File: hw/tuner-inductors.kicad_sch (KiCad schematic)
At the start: 19 parts, among them K1701 G2RL-2, K1702 G2RL-2, K1703 G2RL-2, K1704 G2RL-2, K1705 G2RL-2, K1706 G2RL-2, K1707 G2RL-2, U1701 TPIC6C595PWR

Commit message: I think I have finished the relay conversion and 5V SPI I/O expander crap
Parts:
- removed C1701, C1702, C1703: 10uF, Capacitor_SMD:C_0805_2012Metric, symbol Device:C
- removed K1701, K1702, K1703, K1704, K1705, K1706, K1707: G2RL-2, Library:Relay_DPDT_Omron_G2RL-2, symbol Library:G2RL-2-functional
- removed L1706: 1uH, Library:Coilcraft-uni10, symbol Device:L_Small
- added D7707, D7708, D7709, D7710, D7711, D7712, D7713: 1N4148W, Diode_SMD:D_SOD-123, symbol Diode:1N4148W
- added K7718, K7719, K7720, K7721, K7722, K7723, K7724: G5Q-14-05, Relay_THT:Relay_SPDT_Omron-G5Q-1, symbol Relay:G5Q-1
- added L7730: 1uH, Library:Coilcraft-uni10, symbol Device:L_Small
- renumbered C7720 to C7890, L1701 to L7725, L1702 to L7726, L1703 to L7727, L1704 to L7728, L1705 to L7729, L1707 to L7731, U1701 to U7741
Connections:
- net +5V: now also D7707.1 (K), D7708.1 (K), D7709.1 (K), D7710.1 (K), D7711.1 (K), D7712.1 (K), D7713.1 (K), K7718.5, K7719.5, K7720.5, K7721.5, K7722.5, K7723.5, K7724.5
- net Lcold: now also K7724.4
- net Lhot: now also K7718.2
- net L4: now reaches U7741.11 (DRAIN4)
- net L4: now also D7709.2 (A), K7720.1
- net at L7725.2, L7726.1: now also K7718.4, K7719.2
- net at L7726.2, L7727.1: now also K7719.4, K7720.2
- net at L7728.2, L7729.1: now also K7721.4, K7722.2
- net at L7729.2: now also K7722.4, K7723.2, L7730.1
- net L6: now reaches U7741.13 (DRAIN6)
- net at L7731.1: now also K7723.4, K7724.2, L7730.2
- net at L7727.2, L7728.1: now also K7720.4, K7721.2
- net L5: now reaches U7741.12 (DRAIN5)
- net L5: now also D7708.2 (A), K7719.1
- net L0: now reaches U7741.3 (DRAIN0)
- net L0: now also D7713.2 (A), K7724.1
- net L1: now reaches U7741.4 (DRAIN1)
- net L1: now also D7712.2 (A), K7723.1
- net L2: now reaches U7741.5 (DRAIN2)
- net L2: now also D7711.2 (A), K7722.1
- net L3: now reaches U7741.6 (DRAIN3)
- net L3: now also D7710.2 (A), K7721.1
- new net: D7707.2 (A), K7718.1
- no-connect marks 29 -> 8
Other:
- note removed: "L0"
- note removed: "L1"
- note removed: "L2"
- note removed: "L3"
- note removed: "L4"
- note removed: "L5"
- note removed: "L6"
- moved on the sheet: C7890, L7725, L7726, L7727, L7728, L7729, L7731, U7741

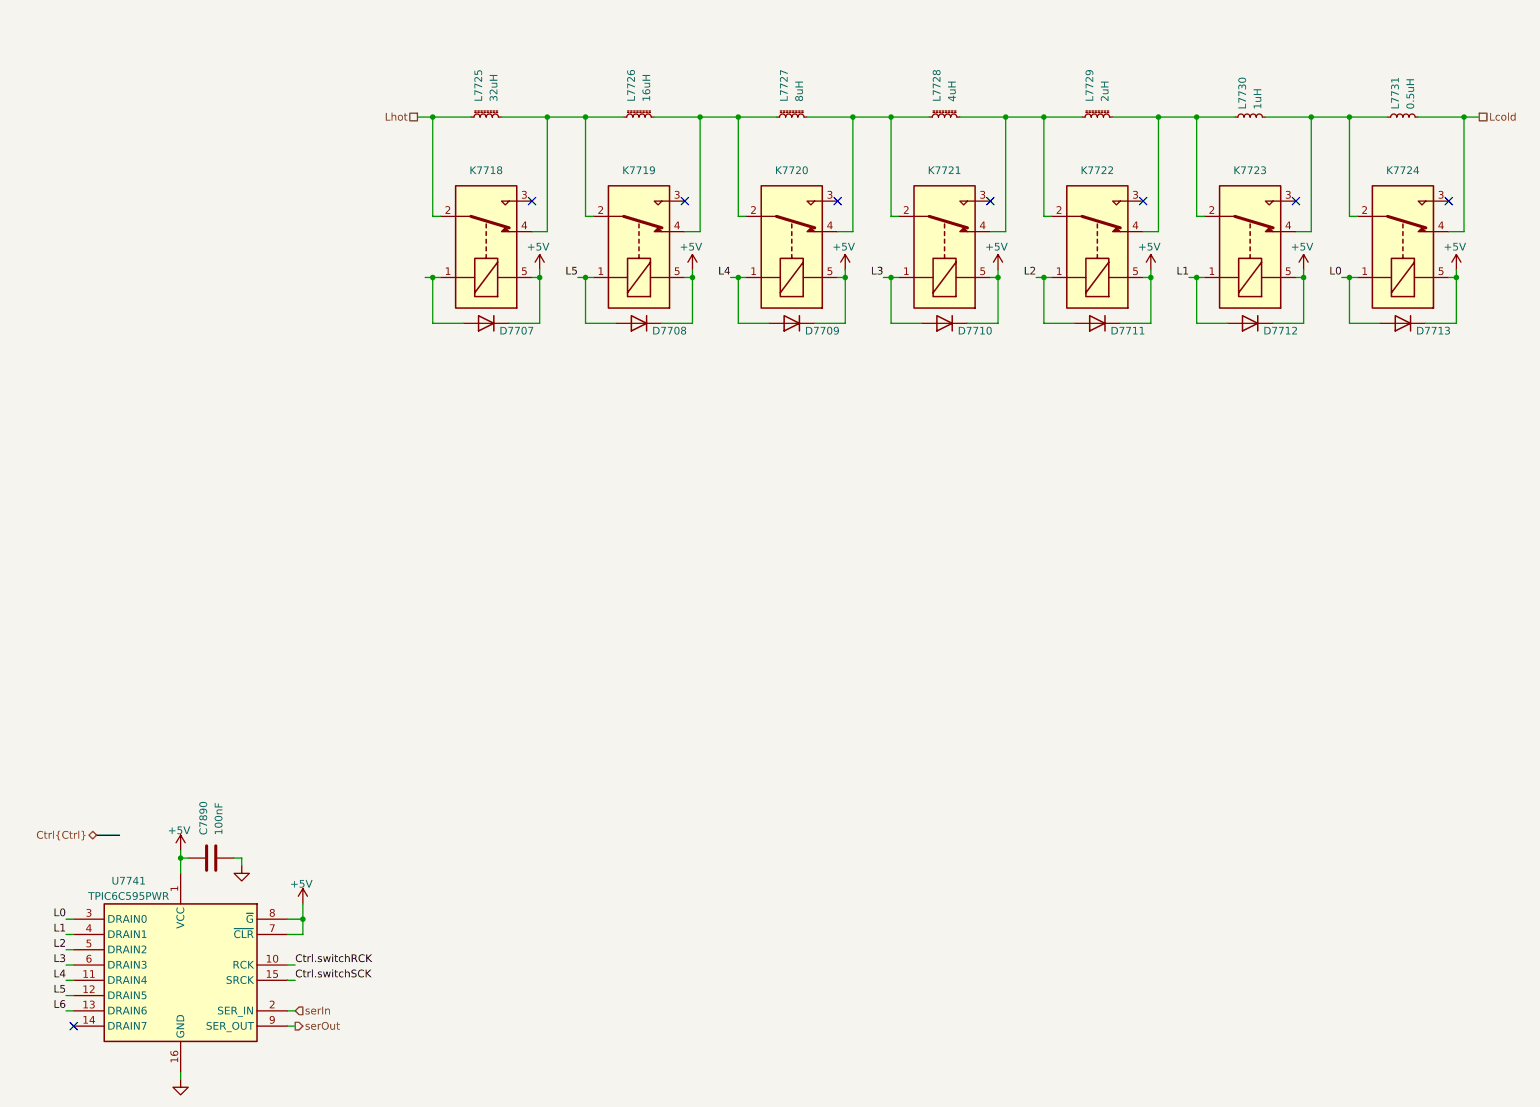
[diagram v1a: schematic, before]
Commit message: Starting to build guanella transformers. Mostly converted to 1-2-1 tx, but FPGA still to do.
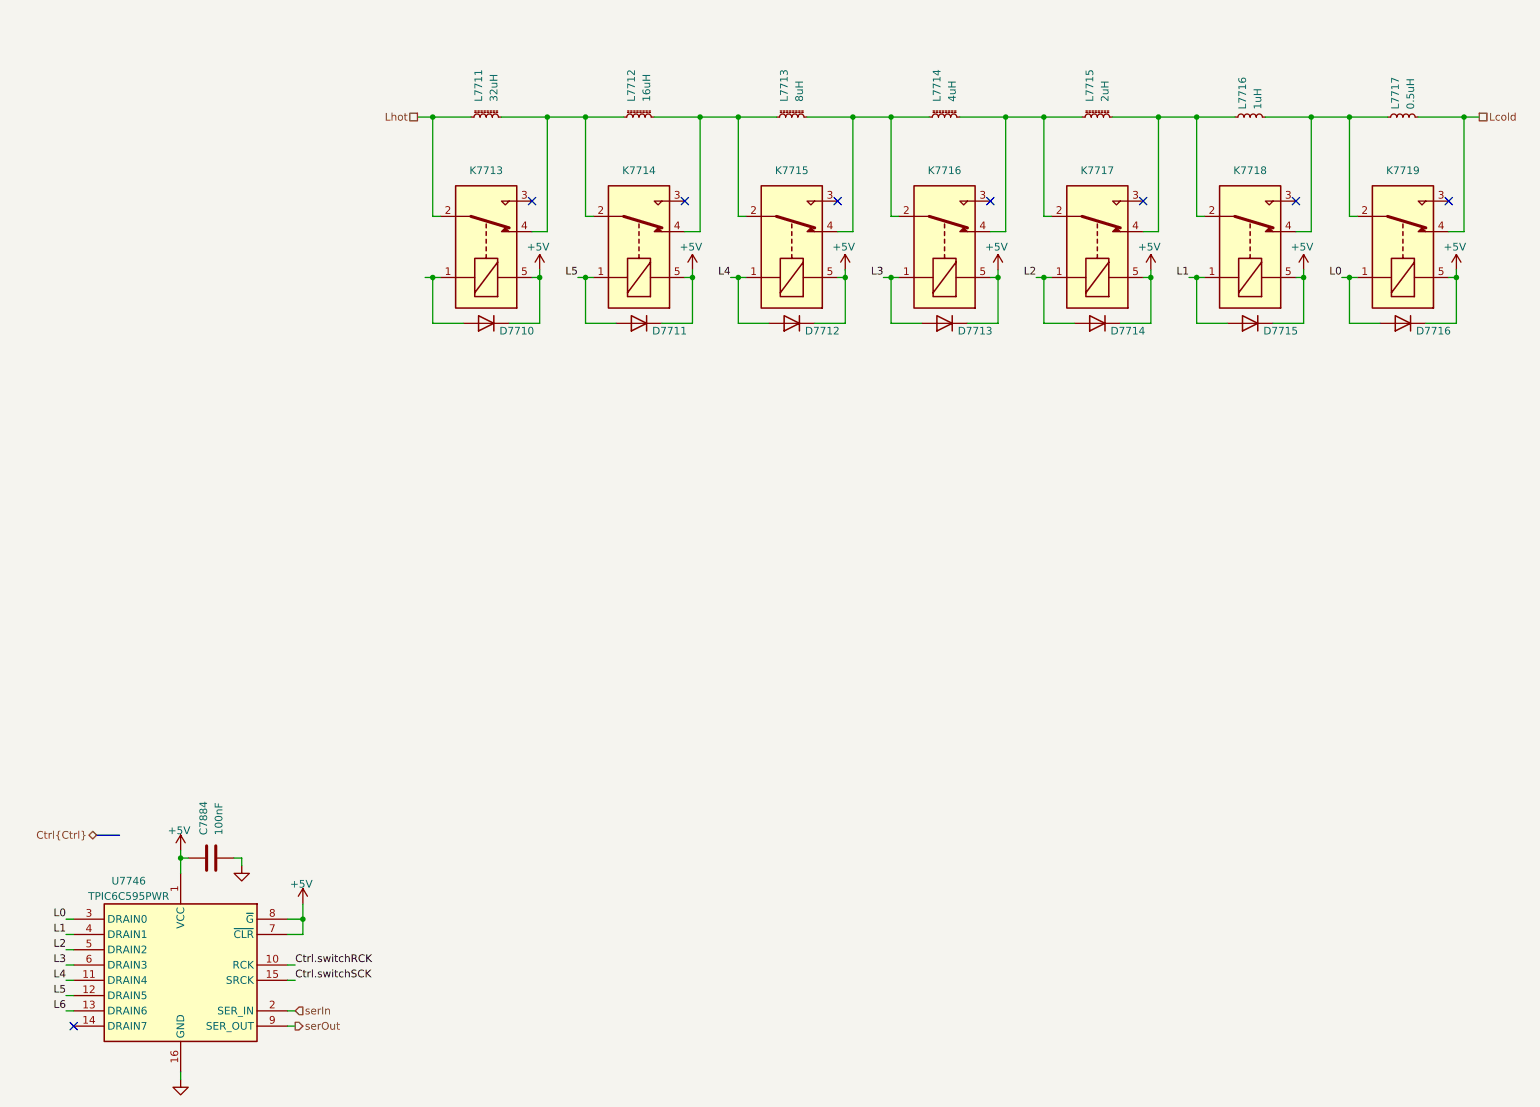
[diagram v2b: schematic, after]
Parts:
- renumbered C7890 to C7884, D7707 to D7710, D7708 to D7711, D7709 to D7712, D7710 to D7713, D7711 to D7714, D7712 to D7715, D7713 to D7716, K7718 to K7713, K7719 to K7714, K7720 to K7715, K7721 to K7716, K7722 to K7717, K7723 to K7718, K7724 to K7719, L7725 to L7711, L7726 to L7712, L7727 to L7713, L7728 to L7714, L7729 to L7715, L7730 to L7716, L7731 to L7717, U7741 to U7746

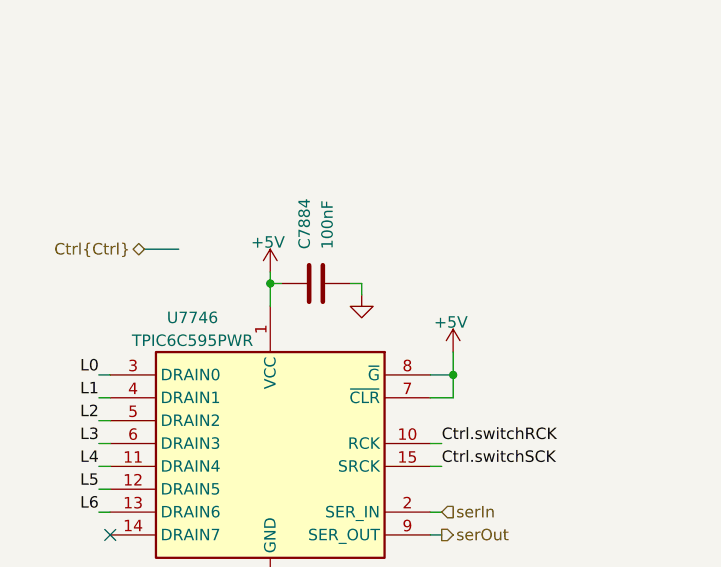
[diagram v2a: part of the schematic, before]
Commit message: Checkpoint. FPGA is mostly done (need a check!). Working on new LPFs. Need inductor footprints and to fix a bunch of broken/missing footprints.
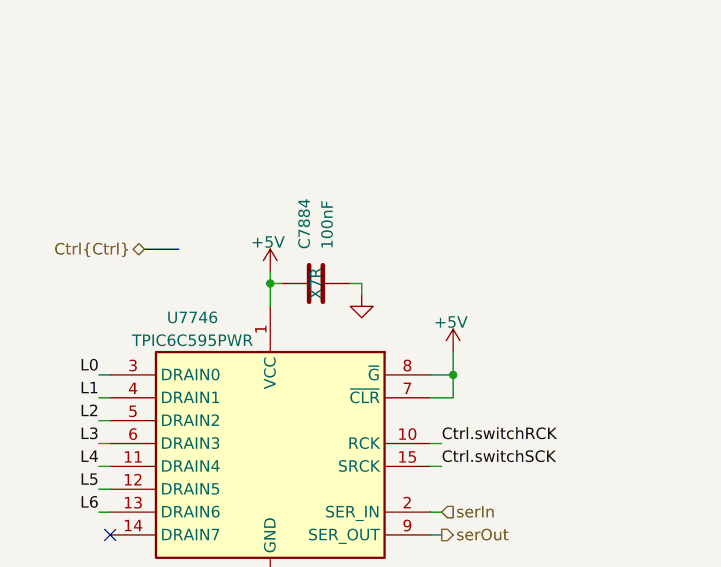
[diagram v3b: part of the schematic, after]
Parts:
- C7884: cap-type (none) -> X7R
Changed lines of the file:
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@@
 			)
 		)
-		(property "cap-type" ""
+		(property "cap-type" "X7R"
 			(at 44.45 162.56 0)
 			(effects

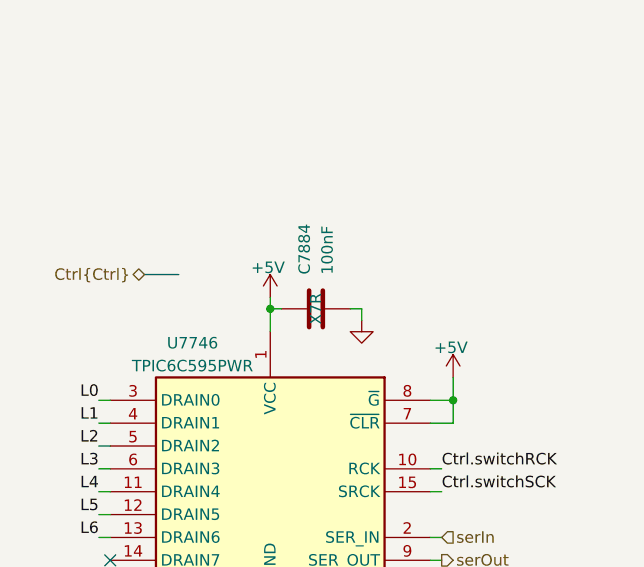
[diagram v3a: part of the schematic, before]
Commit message: OK I have part numbers for consolidated caps, resistors, inductors and all ICs are now Uxxx refdes.
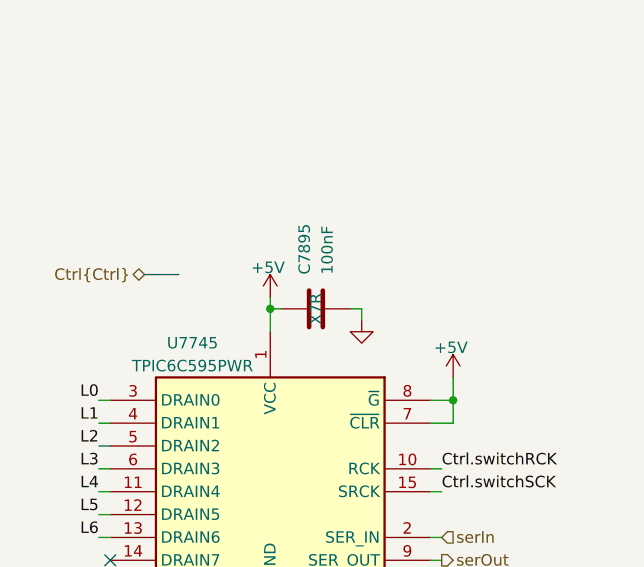
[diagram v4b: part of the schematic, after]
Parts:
- C7895: renamed from C7884; Manufacturer_Name (none) -> Kemet; Manufacturer_Part_Number (none) -> C0805F104K1RACAUTO; Mouser Part Number (none) -> 80-C0805F104K1RAUTO; working-voltage 10V -> 50V
- renumbered U7746 to U7745
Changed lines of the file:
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@@
 		(dnp no)
 		(fields_autoplaced yes)
-		(property "Reference" "#PWR07968"
+		(property "Reference" "#PWR07990"
 			(at 39.37 205.74 0)
 			(effects
@@
 			(project "NexRig"
 				(path "/8ae46c04-d01a-4756-8774-512b694bfaff/2406d03c-531b-4eaf-8b4b-4b266b9d0f2b/99bbdde6-e23e-4e3f-9a6c-8b2d863ddc64/99065376-3804-4997-bf5b-41fcd6e501f1"
-					(reference "#PWR07968")
+					(reference "#PWR07990")
 					(unit 1)
 				)
@@
 		(on_board yes)
 		(dnp no)
-		(property "Reference" "#PWR07973"
+		(property "Reference" "#PWR07995"
 			(at 149.86 68.58 0)
 			(effects
@@
 			(project "NexRig"
 				(path "/8ae46c04-d01a-4756-8774-512b694bfaff/2406d03c-531b-4eaf-8b4b-4b266b9d0f2b/99bbdde6-e23e-4e3f-9a6c-8b2d863ddc64/99065376-3804-4997-bf5b-41fcd6e501f1"
-					(reference "#PWR07973")
+					(reference "#PWR07995")
 					(unit 1)
 				)
@@
 		(dnp no)
 		(fields_autoplaced yes)
-		(property "Reference" "#PWR07969"
+		(property "Reference" "#PWR07991"
 			(at 49.53 170.18 0)
 			(effects
@@
 			(project "NexRig"
 				(path "/8ae46c04-d01a-4756-8774-512b694bfaff/2406d03c-531b-4eaf-8b4b-4b266b9d0f2b/99bbdde6-e23e-4e3f-9a6c-8b2d863ddc64/99065376-3804-4997-bf5b-41fcd6e501f1"
-					(reference "#PWR07969")
+					(reference "#PWR07991")
 					(unit 1)
 				)
@@
 		(on_board yes)
 		(dnp no)
-		(property "Reference" "#PWR07970"
+		(property "Reference" "#PWR07992"
 			(at 59.69 173.99 0)
 			(effects
@@
 			(project "NexRig"
 				(path "/8ae46c04-d01a-4756-8774-512b694bfaff/2406d03c-531b-4eaf-8b4b-4b266b9d0f2b/99bbdde6-e23e-4e3f-9a6c-8b2d863ddc64/99065376-3804-4997-bf5b-41fcd6e501f1"
-					(reference "#PWR07970")
+					(reference "#PWR07992")
 					(unit 1)
 				)
@@
 		(on_board yes)
 		(dnp no)
-		(property "Reference" "C7884"
+		(property "Reference" "C7895"
 			(at 43.1799 158.75 0)
 			(effects
@@
 			)
 		)
-		(property "working-voltage" "10V"
+		(property "working-voltage" "50V"
 			(at 44.45 162.56 0)
 			(effects
@@
 			)
 		)
+		(property "Manufacturer_Name" "Kemet"
+			(at 44.45 162.56 0)
+			(effects
+				(font
+					(size 1.27 1.27)
+				)
+				(hide yes)
+			)
+		)
+		(property "Manufacturer_Part_Number" "C0805F104K1RACAUTO"
+			(at 44.45 162.56 0)
+			(effects
+				(font
+					(size 1.27 1.27)
+				)
+				(hide yes)
+			)
+		)
+		(property "Mouser Part Number" "80-C0805F104K1RAUTO"
+			(at 44.45 162.56 0)
+			(effects
+				(font
+					(size 1.27 1.27)
+				)
+				(hide yes)
+			)
+		)
 		(pin "2"
 		)
@@
 			(project "NexRig"
 				(path "/8ae46c04-d01a-4756-8774-512b694bfaff/2406d03c-531b-4eaf-8b4b-4b266b9d0f2b/99bbdde6-e23e-4e3f-9a6c-8b2d863ddc64/99065376-3804-4997-bf5b-41fcd6e501f1"
-					(reference "C7884")
+					(reference "C7895")
 					(unit 1)
 				)
@@
 		(on_board yes)
 		(dnp no)
-		(property "Reference" "U7746"
+		(property "Reference" "U7745"
 			(at 30.734 166.37 0)
 			(effects
@@
 			(project "NexRig"
 				(path "/8ae46c04-d01a-4756-8774-512b694bfaff/2406d03c-531b-4eaf-8b4b-4b266b9d0f2b/99bbdde6-e23e-4e3f-9a6c-8b2d863ddc64/99065376-3804-4997-bf5b-41fcd6e501f1"
-					(reference "U7746")
+					(reference "U7745")
 					(unit 1)
 				)
@@
 		(on_board yes)
 		(dnp no)
-		(property "Reference" "#PWR07967"
+		(property "Reference" "#PWR07989"
 			(at 39.37 165.1 0)
 			(effects
@@
 			(project "NexRig"
 				(path "/8ae46c04-d01a-4756-8774-512b694bfaff/2406d03c-531b-4eaf-8b4b-4b266b9d0f2b/99bbdde6-e23e-4e3f-9a6c-8b2d863ddc64/99065376-3804-4997-bf5b-41fcd6e501f1"
-					(reference "#PWR07967")
+					(reference "#PWR07989")
 					(unit 1)
 				)
@@
 		(on_board yes)
 		(dnp no)
-		(property "Reference" "#PWR07976"
+		(property "Reference" "#PWR07998"
 			(at 226.06 68.58 0)
 			(effects
@@
 			(project "NexRig"
 				(path "/8ae46c04-d01a-4756-8774-512b694bfaff/2406d03c-531b-4eaf-8b4b-4b266b9d0f2b/99bbdde6-e23e-4e3f-9a6c-8b2d863ddc64/99065376-3804-4997-bf5b-41fcd6e501f1"
-					(reference "#PWR07976")
+					(reference "#PWR07998")
 					(unit 1)
 				)
@@
 		(on_board yes)
 		(dnp no)
-		(property "Reference" "#PWR07974"
+		(property "Reference" "#PWR07996"
 			(at 175.26 68.58 0)
 			(effects
@@
 			(project "NexRig"
 				(path "/8ae46c04-d01a-4756-8774-512b694bfaff/2406d03c-531b-4eaf-8b4b-4b266b9d0f2b/99bbdde6-e23e-4e3f-9a6c-8b2d863ddc64/99065376-3804-4997-bf5b-41fcd6e501f1"
-					(reference "#PWR07974")
+					(reference "#PWR07996")
 					(unit 1)
 				)
@@
 		(on_board yes)
 		(dnp no)
-		(property "Reference" "#PWR07977"
+		(property "Reference" "#PWR07999"
 			(at 251.46 68.58 0)
 			(effects
@@
 			(project "NexRig"
 				(path "/8ae46c04-d01a-4756-8774-512b694bfaff/2406d03c-531b-4eaf-8b4b-4b266b9d0f2b/99bbdde6-e23e-4e3f-9a6c-8b2d863ddc64/99065376-3804-4997-bf5b-41fcd6e501f1"
-					(reference "#PWR07977")
+					(reference "#PWR07999")
 					(unit 1)
 				)
@@
 		(on_board yes)
 		(dnp no)
-		(property "Reference" "#PWR07972"
+		(property "Reference" "#PWR07994"
 			(at 124.46 68.58 0)
 			(effects
@@
 			(project "NexRig"
 				(path "/8ae46c04-d01a-4756-8774-512b694bfaff/2406d03c-531b-4eaf-8b4b-4b266b9d0f2b/99bbdde6-e23e-4e3f-9a6c-8b2d863ddc64/99065376-3804-4997-bf5b-41fcd6e501f1"
-					(reference "#PWR07972")
+					(reference "#PWR07994")
 					(unit 1)
 				)
@@
 		(on_board yes)
 		(dnp no)
-		(property "Reference" "#PWR07971"
+		(property "Reference" "#PWR07993"
 			(at 99.06 68.58 0)
 			(effects
@@
 			(project "NexRig"
 				(path "/8ae46c04-d01a-4756-8774-512b694bfaff/2406d03c-531b-4eaf-8b4b-4b266b9d0f2b/99bbdde6-e23e-4e3f-9a6c-8b2d863ddc64/99065376-3804-4997-bf5b-41fcd6e501f1"
-					(reference "#PWR07971")
+					(reference "#PWR07993")
 					(unit 1)
 				)
@@
 		(on_board yes)
 		(dnp no)
-		(property "Reference" "#PWR07975"
+		(property "Reference" "#PWR07997"
 			(at 200.66 68.58 0)
 			(effects
@@
 			(project "NexRig"
 				(path "/8ae46c04-d01a-4756-8774-512b694bfaff/2406d03c-531b-4eaf-8b4b-4b266b9d0f2b/99bbdde6-e23e-4e3f-9a6c-8b2d863ddc64/99065376-3804-4997-bf5b-41fcd6e501f1"
-					(reference "#PWR07975")
+					(reference "#PWR07997")
 					(unit 1)
 				)

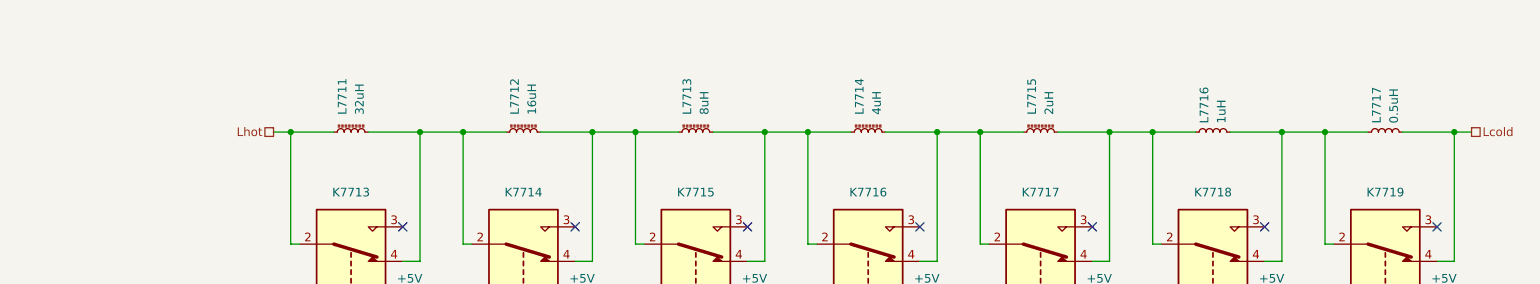
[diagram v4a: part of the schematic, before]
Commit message: Clean up some footprints no longer used. Build footprints for LPF and antenna tuner inductors.
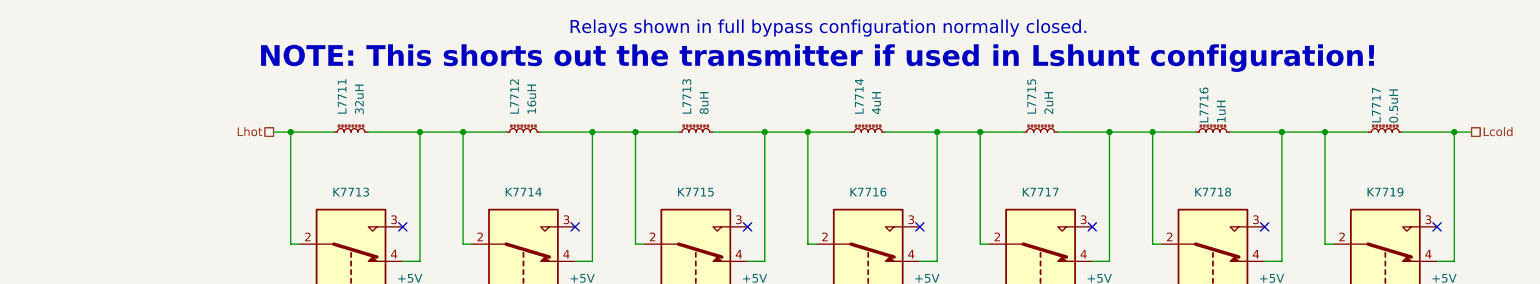
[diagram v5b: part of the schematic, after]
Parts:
- L7711: footprint Inductor_THT:L_Toroid_Vertical_L35.1mm_W21.1mm_P18.50mm_Vishay_TJ6 -> Library:T130-toroid-1-rolling-tire; Core 2 x T80-2 -> T130-2; Winding 54t #24AWG rolling tire mount -> 54t #22AWG rolling tire mount
- L7712: footprint Inductor_THT:L_Toroid_Vertical_L35.1mm_W21.1mm_P18.50mm_Vishay_TJ6 -> Library:T106-toroid-1-rolling-tire; Core T80-2 -> T106-2; Winding 54t #24AWG flat mount -> 35t #22AWG rolling tire
- L7713: footprint Inductor_THT:L_Toroid_Vertical_L26.7mm_W14.0mm_P10.16mm_Pulse_D -> Library:T80-toroid-1-rolling-tire; Winding 38t #24AWG mount flat -> 38t #22AWG mount flat
- L7714: footprint Inductor_THT:L_Toroid_Vertical_L26.7mm_W14.0mm_P10.16mm_Pulse_D -> Library:T80-toroid-1-rolling-tire; Core T50-2 -> T80-2; Winding 29t #24AWG -> 38t #22AWG
- L7715: footprint Inductor_THT:L_Toroid_Vertical_L26.7mm_W14.0mm_P10.16mm_Pulse_D -> Library:T68-toroid-1-rolling-tire; Core T50-2 -> T68-6; Winding 21t #24AWG -> 21t #22AWG
- L7716: footprint Library:Coilcraft-uni10 -> Library:T50-toroid-1-rolling-tire; symbol Device:L_Small -> Device:L_Ferrite_Small; Mfg Coilcraft -> (none); MfgPN 143-20L -> (none)
- L7717: footprint Library:Coilcraft-uni10 -> Library:T50-toroid-1-rolling-tire; symbol Device:L_Small -> Device:L_Ferrite_Small; Mfg Coilcraft -> (none); MfgPN 143-11L -> (none)
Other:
- note added: "NOTE: This shorts out the transmitter if used in Lshunt configuration!"
- note added: "Relays shown in full bypass configuration normally closed."
